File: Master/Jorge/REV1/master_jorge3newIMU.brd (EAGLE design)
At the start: 71.7 x 73.6 mm, 62 parts, among them J1 ISP, K1 653002114822, K2 653002114822, K3 653002114822, K4 653002114822, U1 ATMEGA128RFA1, U2 TPS73633-DBVT, U3 SI2366DS-T1-GE3, U4 LSM9DS0, U5 SI2366DS-T1-GE3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

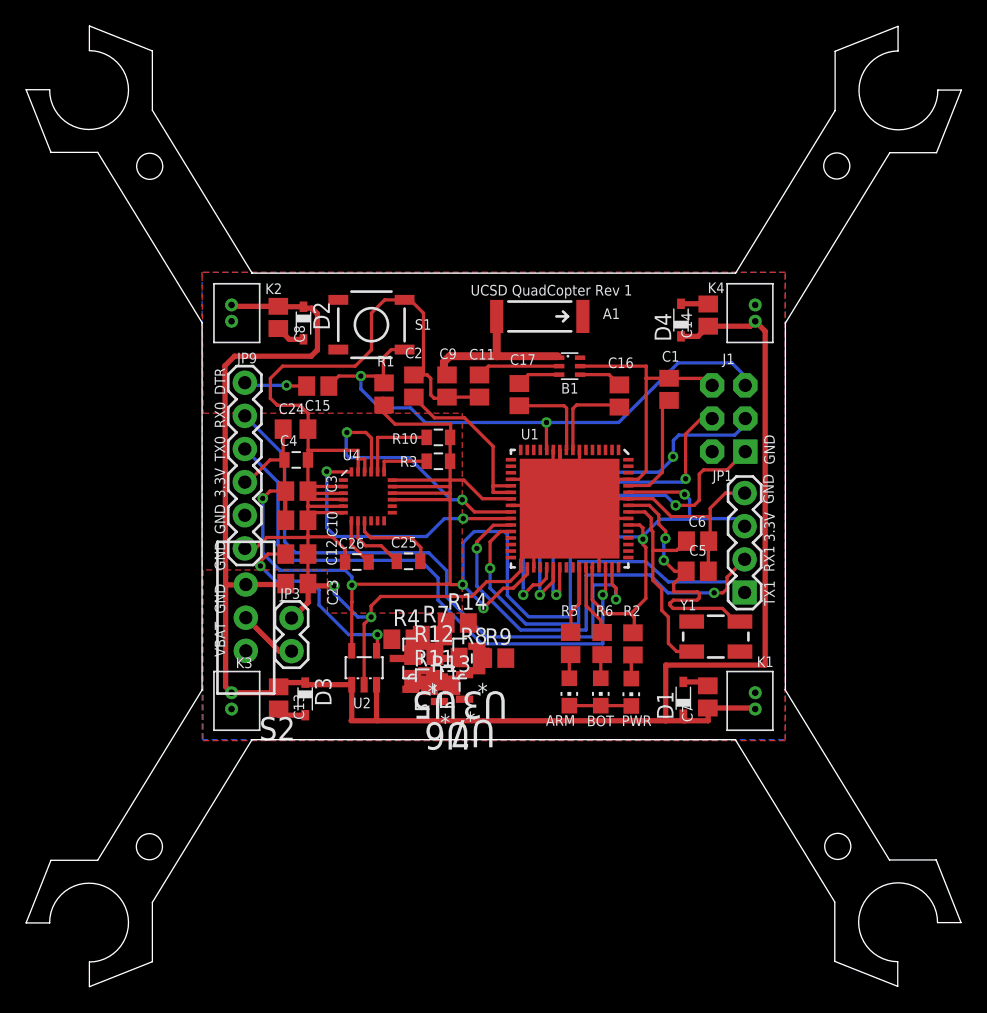
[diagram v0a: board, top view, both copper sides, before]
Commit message: Finish routing REV1
Just missing increase arm size for motors.
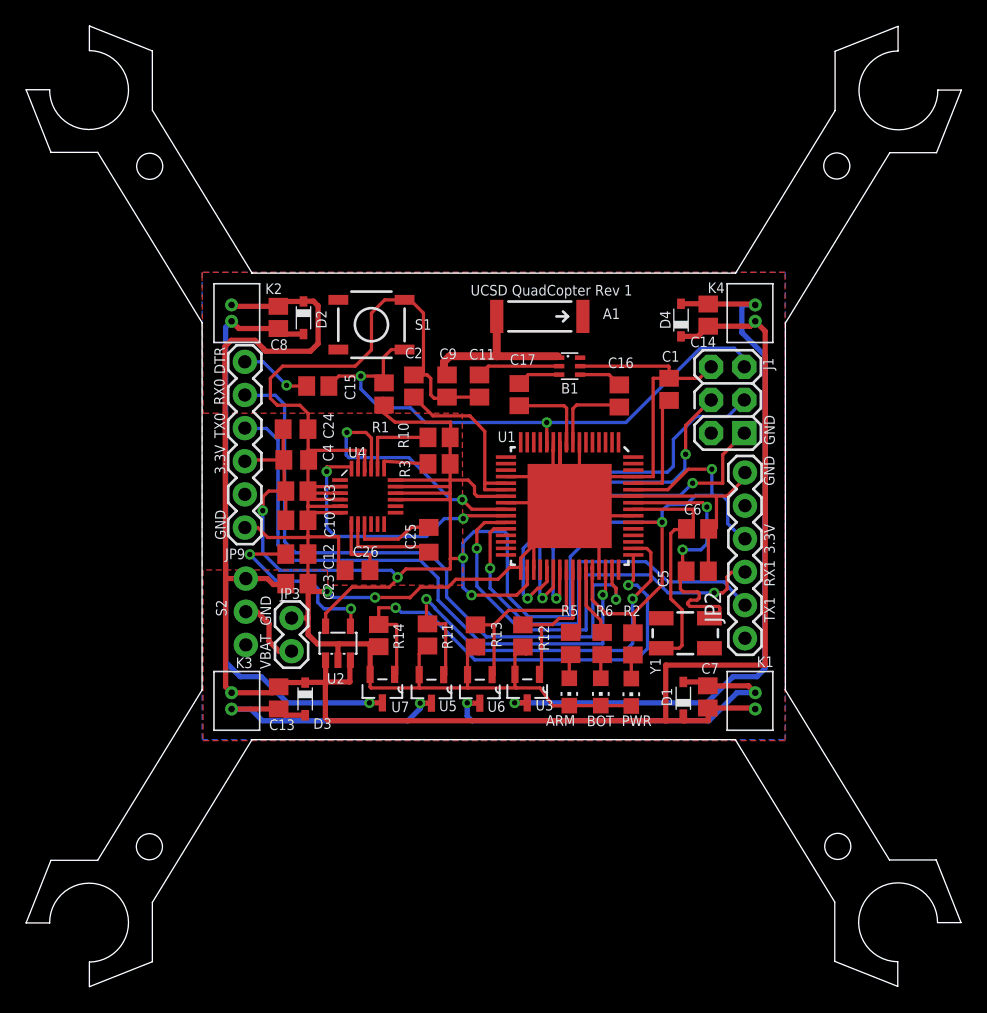
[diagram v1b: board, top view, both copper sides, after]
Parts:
- removed JP1: Debugger, SparkFun-Connectors:1X04
- removed R4, R7, R8, R9: 100, resistor:R0805
- added JP2: FTDI, SparkFun-Connectors:FTDI_BASIC
- C25, C26, C4: device SparkFun-Capacitors:0805 -> rcl:C0805
- D1, D2, D3, D4: value BAT60J -> BAS16WS; device diode:SOD323_ST -> Controller:SOD323_ST
- J1: device SparkFun-Connectors:2X3-NS -> Controller:2X3-NS
- R10, R3: device SparkFun-Passives:0805 -> resistor:R0805
- S2: value (none) -> SW; device SparkFun-Electromechanical:SWITCH-SPDT -> Controller:SWITCH-SPDT
- U1: device SparkFun-DigitalIC:QFN-64 -> Controller:QFN-64
- U3, U5, U6, U7: value SI2366DS-T1-GE3 -> SI2302CDS-T1-E3; device Vishay_By_element14_Batch_1:SOT95P237X112-3N -> Controller:SOT95P237X112-3N
- U4: device IMU_parts:LGA-24 -> Controller:LGA-24
- moved R12 7.74 mm to (24.6, 7.95), turned to 270 degrees
- moved R14 6.10 mm to (13.5, 7.98), turned to 270 degrees
- moved U3 5.47 mm to (24.9, 3.91), turned to 270 degrees
- moved U7 5.21 mm to (13.8, 3.91), turned to 270 degrees
- moved R13 4.63 mm to (21.0, 7.95), turned to 270 degrees
- moved U6 4.19 mm to (21.3, 3.89), turned to 270 degrees
- moved R11 3.44 mm to (17.3, 8.03), turned to 270 degrees
- moved U2 2.75 mm to (10.4, 7.39)
- moved U5 2.75 mm to (17.6, 3.89), turned to 270 degrees
- moved Y1 2.35 mm to (37.0, 8.15)
- moved C25 2.26 mm to (17.4, 15.3), turned to 270 degrees
- moved JP9 1.60 mm to (3.28, 29.0)
- moved J1 1.42 mm to (40.3, 26.0)
- moved C6 0.94 mm to (38.0, 16.2)
- moved C26 0.64 mm to (11.9, 13.0)
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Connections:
- removed net N$12: R14.1, R9.1, U7.1
- removed net N$14: C7.2, D1.A
- removed net N$19: C13.2, D3.A
- removed net N$27: C14.2, D4.A
- removed net N$5: R11.1, R4.1, U5.1
- removed net N$6: R12.1, R7.1, U3.1
- removed net N$9: R13.1, R8.1, U6.1
- net 3.3V: now also JP2.VCC; no longer JP1.3
- net GND: now also JP2.GND; no longer JP1.4
- net N$29: now also C7.2, D1.A
- net N$31: now also C13.2, D3.A
- net N$32: now also C14.2, D4.A
- net PB4: now also R13.1, U6.1; no longer R8.2
- net PB5: now also R12.1, U3.1; no longer R7.2
- net PE3: now also R14.1, U7.1; no longer R9.2
- net PE4: now also R11.1, U5.1; no longer R4.2
- net RX1: now also JP2.TXO; no longer JP1.2
- net TX1: now also JP2.RXI; no longer JP1.1
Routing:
- net N$32: track 0.10 -> 56.6 mm, vias 0 -> 1
- net GND: track 199.7 -> 246.1 mm
- net N$30: track 2.27 -> 45.5 mm, vias 0 -> 1
- net PE3: track 0.00 -> 37.5 mm, vias 0 -> 2
- net PE4: track 0.00 -> 35.5 mm, vias 0 -> 2
- net N$29: track 0.00 -> 31.0 mm, vias 0 -> 1
- net N$31: track 0.00 -> 22.3 mm, vias 0 -> 1
- net PB4: track 0.00 -> 14.5 mm
- net PB5: track 0.00 -> 11.7 mm
- net 3.3V: track 147.7 -> 154.8 mm
- net VBAT: track 140.5 -> 145.3 mm
- net N$21: track 5.04 -> 7.87 mm
- net TX0: track 48.1 -> 50.8 mm
- net N$19: track 2.51 -> 0.00 mm
- net RX0: track 43.4 -> 45.8 mm
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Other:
- board text added: ">Info Board Name: UCSD QuadCopter Part Number: 0 Number of Layers: 2 Dimension X= 2.83 inch Dimension Y= 2.90 inch Board Material Type: FR-4 Solder Mask Color: Green Silkscreen Color: White Finish Plating: HASAL Revision Number: 1"
- board text removed: ">Info Board Name: UCSDQuadCop Part Number: 0 Number of Layers: 2 Dimension X= 2.83 inch Dimension Y= 2.90 inch Board Material Type: FR-4 Solder Mask Color: Red Silkscreen Color: White Finish Plating: HASAL Revision Number: 0"
